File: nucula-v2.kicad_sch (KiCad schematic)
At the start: 0 parts

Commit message: Draft ESP32-C3 USB-C and Li-ion power schematic
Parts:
- added C1, C2, C4, C5, C6, C9: 22uF, Capacitor_SMD:C_0805_2012Metric, symbol Device:C
- added C10, C11, C13, C14: 100nF, Capacitor_SMD:C_0603_1608Metric, symbol Device:C
- added C12: 1uF, Capacitor_SMD:C_0603_1608Metric, symbol Device:C
- added C3: 22pF, Capacitor_SMD:C_0603_1608Metric, symbol Device:C
- added C7, C8: DNP / USB tune, Capacitor_SMD:C_0603_1608Metric, symbol Device:C
- added D1, D2: SS14, Diode_SMD:D_SMA, symbol Device:D_Schottky
- added D3: CHARGE (red), LED_SMD:LED_0603_1608Metric, symbol Device:LED
- added J1: USB4105-GF-A, Connector_USB:USB_C_Receptacle_GCT_USB4105-xx-A_16P_TopMnt_Horizontal, symbol Connector:USB_C_Receptacle_USB2.0_16P
- added J2: JST-PH / 1S Li-ion, Connector_JST:JST_PH_B2B-PH-K_1x02_P2.00mm_Vertical, symbol Connector_Generic:Conn_01x02
- added L1: 2.2uH, Nucula_Project:L_Taiyo-Yuden_NR-30xx, symbol Device:L
- added Q1: IRLML6402, Package_TO_SOT_SMD:SOT-23, symbol Transistor_FET:IRLML6402
- added Q2: BSS138, Package_TO_SOT_SMD:SOT-23, symbol Transistor_FET:BSS138
- added R1, R2: 5.1k, Resistor_SMD:R_0603_1608Metric, symbol Device:R
- added R10, R11, R3, R5, R8, R9: 10k, Resistor_SMD:R_0603_1608Metric, symbol Device:R
- added R12, R13: 22R, Resistor_SMD:R_0603_1608Metric, symbol Device:R
- added R14: 100R, Resistor_SMD:R_0603_1608Metric, symbol Device:R
- added R15, R16: 470k, Resistor_SMD:R_0603_1608Metric, symbol Device:R
- added R17, R18: 100k, Resistor_SMD:R_0603_1608Metric, symbol Device:R
- added R4: 2.2k, Resistor_SMD:R_0603_1608Metric, symbol Device:R
- added R6: 220k, Resistor_SMD:R_0603_1608Metric, symbol Device:R
- added R7: 48.7k, Resistor_SMD:R_0603_1608Metric, symbol Device:R
- added SW1: RESET, Button_Switch_SMD:SW_SPST_B3U-1000P, symbol Switch:SW_Push
- added SW2: BOOT, Button_Switch_SMD:SW_SPST_B3U-1000P, symbol Switch:SW_Push
- added U1: TP4054-42-SOT235, Package_TO_SOT_SMD:SOT-23-5, symbol Nucula_Project:TP4054-42-SOT235
- added U2: SY8089AAAC, Package_TO_SOT_SMD:SOT-23-5, symbol Nucula_Project:SY8089AAAC
- added U3: ESP32-C3-WROOM-02-N4, Nucula_Project:ESP32-C3-WROOM-02-N4, symbol Nucula_Project:ESP32-C3-WROOM-02-N4
- added U4: USBLC6-2SC6, Package_TO_SOT_SMD:SOT-23-6, symbol Power_Protection:USBLC6-2SC6
- added U5: TLV803EA30DCKR, Package_TO_SOT_SMD:SOT-323_SC-70, symbol Nucula_Project:TLV803EA30DCKR
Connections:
- new net: C8.1, R13.2, U3.14 (IO19)
- new net: L1.1, U2.3 (LX)
- new net: C7.1, R12.2, U3.13 (IO18)
- new net: J1.A5 (CC1), R1.1
- new net: J1.B5 (CC2), R2.1
- new net: R4.1, U1.1 (~{CHRG})
- new net: R3.1, U1.5 (PROG)
- new net: D3.1 (K), R4.2
- new net: R14.2, SW2.1
- new net +3V3: C10.1, C11.1, C3.1, C5.1, C6.1, C9.1, L1.2, R10.1, R11.1, R17.1, R6.1, R8.1, R9.1, U3.1 (3V3), U5.3 (VDD)
- new net BOOT_N: R11.2, R14.1, U3.8 (IO9)
- new net BUCK_FB: C3.2, R6.2, R7.1, U2.5 (FB)
- new net ESP_EN: C12.1, R8.2, SW1.1, U3.2 (EN), U5.2 (~{RESET})
- new net GND: C1.2, C10.2, C11.2, C12.2, C13.2, C14.2, C2.2, C4.2, C5.2, C6.2, C7.2, C8.2, C9.2, J1.A1 (GND), J1.A12 (GND), J1.B1 (GND), J1.B12 (GND), J1.SH (SHIELD), J2.2 (Pin_2), Q2.2 (S), R1.2, R16.2, R18.2, R2.2, R3.2, R5.2, R7.2, SW1.2, SW2.2, U1.2 (GND), U2.2 (GND), U3.19 (GND), U3.9 (GND), U4.2 (GND), U5.1 (GND)
- new net STRAP_GPIO2: R9.2, U3.16 (IO2)
- new net STRAP_GPIO8: R10.2, U3.7 (IO8)
- new net USB_5V: C1.1, D1.1 (K), D2.2 (A), D3.2 (A), Q1.1 (G), R5.1, U1.4 (VCC)
- new net USB_D+: J1.A6 (D+), J1.B6 (D+), U4.3 (I/O2)
- new net USB_D-: J1.A7 (D-), J1.B7 (D-), U4.1 (I/O1)
- new net USB_ESD_D+: R13.1, U4.4 (I/O2)
- new net USB_ESD_D-: R12.1, U4.6 (I/O1)
- new net USB_PRESENT_N: Q2.3 (D), R17.2, U3.17 (IO1)
- new net VBAT: C2.1, J2.1 (Pin_1), Q1.3 (D), R15.1, U1.3 (BAT)
- new net VBAT_ADC: C13.1, R15.2, R16.1, U3.18 (IO0)
- new net VBUS: C14.1, D1.2 (A), J1.A4 (VBUS), J1.A9 (VBUS), J1.B4 (VBUS), J1.B9 (VBUS), Q2.1 (G), R18.1, U4.5 (VBUS)
- new net VSYS: C4.1, D2.1 (K), Q1.2 (S), U2.1 (EN), U2.4 (IN)
- no-connect marks 0 -> 10
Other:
- note added: "01 USB 2.0 device / 5 V sink"
- note added: "02 4.2 V / 100 mA charger"
- note added: "03 USB-priority supply / 3.31 V buck"
- note added: "04 ESP32-C3-WROOM-02-N4 / native USB"
- note added: "05 Reset, undervoltage and boot straps"
- note added: "06 Battery and USB presence sensing"
- note added: "3.08 V supervisor, open-drain reset, ~200 ms delay. EN: 10k / 1uF. 3.08 V nominal low-voltage reset."
- note added: "CC1 / CC2: independent 5.1k Rd. No USB-PD. Route D+/D- as a 90 ohm differential pair. Place U4 at connector; R12/R13 at module. See design notes for USB current / inrush limits."
- note added: "DRAFT / before PCB: Confirm protected battery and JST polarity. Validate USB current, inrush, suspend and ESD. Verify regulator layout, capacitor bias and load steps. Reference: Olimex ESP32-C3-DevKit-Lipo Rev C. See docs/power-design.md for sources and limits."
- note added: "ERC source declarations"
- note added: "Hold BOOT; tap RESET to enter ROM download mode. GPIO8 must stay high while GPIO9 is low. No large capacitor on GPIO9."
- note added: "NUCULA v2 / USB-C, Li-ion power and ESP32-C3"
- note added: "Protected 1S Li-ion/LiPo only (4.2 V full). J2 pin 1 = BAT+; pin 2 = GND. Check pack polarity! 100 mA nominal; termination ~10 mA. No cell-temperature input. Confirm battery rating."
- note added: "Q1 drain = battery, source = VSYS. Body diode points VBAT -> VSYS. USB load bypasses charge-current sensing."
- note added: "USB D- = GPIO18 (pin 13); D+ = GPIO19 (pin 14). No UART bridge. Unused GPIOs deliberately marked NC. Keep antenna clear; bond EP pin 19 and pin 9 to ground. Use ADC1 GPIO0 for battery sensing (not ADC2)."
- note added: "VBAT_ADC = VBAT / 2, max ~2.15 V incl. tolerances. ADC1 GPIO0: use calibrated 11/12 dB attenuation. Divider load ~4.5 uA; allow >=120 ms to settle. USB_PRESENT_N: GPIO1 LOW when VBUS is present. Firmware must disable USB attach when VBUS is absent. Q2 isolates 5 V VBUS from the 3.3 V GPIO supply."
- note added: "VOUT = 3.31 V; R6 / R7: 0.1% precision 500 mA rail design target; validate transients. Buck only: low battery causes dropout / reset. C5 + C6: 44 uF nominal; verify DC-bias derating."
- title: (none) -> Nucula v2 - USB-C, battery power and ESP32-C3

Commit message: Set 400 mAh battery target with JST-PH connector
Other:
- note added: "Protected 1S LiPo, ~400mAh (3.7V nom / 4.2V full). J2: JST-PH 2.0mm; pin 1 = BAT+; pin 2 = GND. 100mA charge = 0.25C at 400mAh; ~10mA termination. Confirm pack polarity and ratings; no cell-temp input."
- note removed: "Protected 1S Li-ion/LiPo only (4.2 V full). J2 pin 1 = BAT+; pin 2 = GND. Check pack polarity! 100 mA nominal; termination ~10 mA. No cell-temperature input. Confirm battery rating."
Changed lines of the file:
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@@
   (title_block
     (title "Nucula v2 - USB-C, battery power and ESP32-C3")
-    (date "2026-09-19")
+    (date "2026-09-20")
     (rev "A-draft")
     (comment 1 "Adapted from Olimex ESP32-C3-DevKit-Lipo Rev C; CERN-OHL-S-2.0")
@@
     )
   )
-  (text "Protected 1S Li-ion/LiPo only (4.2 V full).\nJ2 pin 1 = BAT+; pin 2 = GND. Check pack polarity!\n100 mA nominal; termination ~10 mA.\nNo cell-temperature input. Confirm battery rating."
+  (text "Protected 1S LiPo, ~400mAh (3.7V nom / 4.2V full).\nJ2: JST-PH 2.0mm; pin 1 = BAT+; pin 2 = GND.\n100mA charge = 0.25C at 400mAh; ~10mA termination.\nConfirm pack polarity and ratings; no cell-temp input."
     (at 144.78 91.44 0)
     (effects

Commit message: Integrate NFC, OLED and breakaway I2C keyboard
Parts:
- removed C1, C2, C4, C5, C6, C9: 22uF, Capacitor_SMD:C_0805_2012Metric, symbol Device:C
- removed C10, C11, C13, C14: 100nF, Capacitor_SMD:C_0603_1608Metric, symbol Device:C
- removed C12: 1uF, Capacitor_SMD:C_0603_1608Metric, symbol Device:C
- removed C3: 22pF, Capacitor_SMD:C_0603_1608Metric, symbol Device:C
- removed C7, C8: DNP / USB tune, Capacitor_SMD:C_0603_1608Metric, symbol Device:C
- removed D1, D2: SS14, Diode_SMD:D_SMA, symbol Device:D_Schottky
- removed D3: CHARGE (red), LED_SMD:LED_0603_1608Metric, symbol Device:LED
- removed J1: USB4105-GF-A, Connector_USB:USB_C_Receptacle_GCT_USB4105-xx-A_16P_TopMnt_Horizontal, symbol Connector:USB_C_Receptacle_USB2.0_16P
- removed J2: JST-PH / 1S Li-ion, Connector_JST:JST_PH_B2B-PH-K_1x02_P2.00mm_Vertical, symbol Connector_Generic:Conn_01x02
- removed L1: 2.2uH, Nucula_Project:L_Taiyo-Yuden_NR-30xx, symbol Device:L
- removed Q1: IRLML6402, Package_TO_SOT_SMD:SOT-23, symbol Transistor_FET:IRLML6402
- removed Q2: BSS138, Package_TO_SOT_SMD:SOT-23, symbol Transistor_FET:BSS138
- removed R1, R2: 5.1k, Resistor_SMD:R_0603_1608Metric, symbol Device:R
- removed R10, R11, R3, R5, R8, R9: 10k, Resistor_SMD:R_0603_1608Metric, symbol Device:R
- removed R12, R13: 22R, Resistor_SMD:R_0603_1608Metric, symbol Device:R
- removed R14: 100R, Resistor_SMD:R_0603_1608Metric, symbol Device:R
- removed R15, R16: 470k, Resistor_SMD:R_0603_1608Metric, symbol Device:R
- removed R17, R18: 100k, Resistor_SMD:R_0603_1608Metric, symbol Device:R
- removed R4: 2.2k, Resistor_SMD:R_0603_1608Metric, symbol Device:R
- removed R6: 220k, Resistor_SMD:R_0603_1608Metric, symbol Device:R
- removed R7: 48.7k, Resistor_SMD:R_0603_1608Metric, symbol Device:R
- removed SW1: RESET, Button_Switch_SMD:SW_SPST_B3U-1000P, symbol Switch:SW_Push
- removed SW2: BOOT, Button_Switch_SMD:SW_SPST_B3U-1000P, symbol Switch:SW_Push
- removed U1: TP4054-42-SOT235, Package_TO_SOT_SMD:SOT-23-5, symbol Nucula_Project:TP4054-42-SOT235
- removed U2: SY8089AAAC, Package_TO_SOT_SMD:SOT-23-5, symbol Nucula_Project:SY8089AAAC
- removed U3: ESP32-C3-WROOM-02-N4, Nucula_Project:ESP32-C3-WROOM-02-N4, symbol Nucula_Project:ESP32-C3-WROOM-02-N4
- removed U4: USBLC6-2SC6, Package_TO_SOT_SMD:SOT-23-6, symbol Power_Protection:USBLC6-2SC6
- removed U5: TLV803EA30DCKR, Package_TO_SOT_SMD:SOT-323_SC-70, symbol Nucula_Project:TLV803EA30DCKR
- added C49: 1uF, Capacitor_SMD:C_0805_2012Metric, symbol Device:C
- added C50: 2.2uF, Capacitor_SMD:C_0805_2012Metric, symbol Device:C
- added J4: MAIN LINK / OPTIONAL, Connector_PinHeader_2.54mm:PinHeader_1x05_P2.54mm_Vertical, symbol Connector_Generic:Conn_01x05
- added R19, R20: 2.2k, Resistor_SMD:R_0603_1608Metric, symbol Device:R
- added R40: 100k, Resistor_SMD:R_0603_1608Metric, symbol Device:R
- added U9: MCP1700T-3002E/TT, Package_TO_SOT_SMD:SOT-23, symbol Regulator_Linear:MCP1700x-300xxTT
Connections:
- net +3V3: now also C49.1, J4.1 (Pin_1), R40.1, U9.3 (VI)
- net GND: now also C49.2, C50.2, J4.2 (Pin_2), U9.1 (GND)
- new net +3V0: C50.1, R19.1, R20.1, U9.2 (VO)
- new net I2C_SCL: J4.4 (Pin_4), R20.2
- new net I2C_SDA: J4.3 (Pin_3), R19.2
- new net KEY_INT_N: J4.5 (Pin_5), R40.2
- no-connect marks 10 -> 0
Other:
- added sheet Keyboard / breakaway / 0x20 (keyboard.kicad_sch)
- added sheet NFC / PN7160 / 0x28 (nfc.kicad_sch)
- added sheet OLED / SSD1309 / 0x3C (oled.kicad_sch)
- added sheet Power + ESP32-C3 (power-mcu.kicad_sch)
- note added: "3.0 V display logic and common I2C pull-ups. SSD1309 logic max = 3.3 V; existing buck worst case ~3.39 V. 3.0 V HIGH levels also meet the 3.3 V devices' thresholds. One populated pair of I2C pull-ups. Bus speed: 100 kHz. No I2C multiplexer is needed; addresses are distinct."
- note added: "Break line carries five nets only. Reconnect J4 <-> J5 after separation. J3 9-pin keyboard header remains DNP. Mechanical break line is deferred to PCB layout."
- note added: "NFC / OLED power comes from VSYS; digital logic from regulated rails. Concurrent Wi-Fi + NFC + OLED can exceed a small 400 mAh pack's rating. Confirm peak battery current and USB input power before PCB release. RF matching/coil and exact OLED flex remain intentionally provisional."
- note added: "NUCULA v2 / system interconnect"
- note removed: "01 USB 2.0 device / 5 V sink"
- note removed: "02 4.2 V / 100 mA charger"
- note removed: "03 USB-priority supply / 3.31 V buck"
- note removed: "04 ESP32-C3-WROOM-02-N4 / native USB"
- note removed: "05 Reset, undervoltage and boot straps"
- note removed: "06 Battery and USB presence sensing"
- note removed: "3.08 V supervisor, open-drain reset, ~200 ms delay. EN: 10k / 1uF. 3.08 V nominal low-voltage reset."
- note removed: "CC1 / CC2: independent 5.1k Rd. No USB-PD. Route D+/D- as a 90 ohm differential pair. Place U4 at connector; R12/R13 at module. See design notes for USB current / inrush limits."
- note removed: "DRAFT / before PCB: Confirm protected battery and JST polarity. Validate USB current, inrush, suspend and ESD. Verify regulator layout, capacitor bias and load steps. Reference: Olimex ESP32-C3-DevKit-Lipo Rev C. See docs/power-design.md for sources and limits."
- note removed: "ERC source declarations"
- note removed: "Hold BOOT; tap RESET to enter ROM download mode. GPIO8 must stay high while GPIO9 is low. No large capacitor on GPIO9."
- note removed: "NUCULA v2 / USB-C, Li-ion power and ESP32-C3"
- note removed: "Protected 1S LiPo, ~400mAh (3.7V nom / 4.2V full). J2: JST-PH 2.0mm; pin 1 = BAT+; pin 2 = GND. 100mA charge = 0.25C at 400mAh; ~10mA termination. Confirm pack polarity and ratings; no cell-temp input."
- note removed: "Q1 drain = battery, source = VSYS. Body diode points VBAT -> VSYS. USB load bypasses charge-current sensing."
- note removed: "USB D- = GPIO18 (pin 13); D+ = GPIO19 (pin 14). No UART bridge. Unused GPIOs deliberately marked NC. Keep antenna clear; bond EP pin 19 and pin 9 to ground. Use ADC1 GPIO0 for battery sensing (not ADC2)."
- note removed: "VBAT_ADC = VBAT / 2, max ~2.15 V incl. tolerances. ADC1 GPIO0: use calibrated 11/12 dB attenuation. Divider load ~4.5 uA; allow >=120 ms to settle. USB_PRESENT_N: GPIO1 LOW when VBUS is present. Firmware must disable USB attach when VBUS is absent. Q2 isolates 5 V VBUS from the 3.3 V GPIO supply."
- note removed: "VOUT = 3.31 V; R6 / R7: 0.1% precision 500 mA rail design target; validate transients. Buck only: low battery causes dropout / reset. C5 + C6: 44 uF nominal; verify DC-bias derating."
- title: Nucula v2 - USB-C, battery power and ESP32-C3 -> Nucula v2 - system interconnect

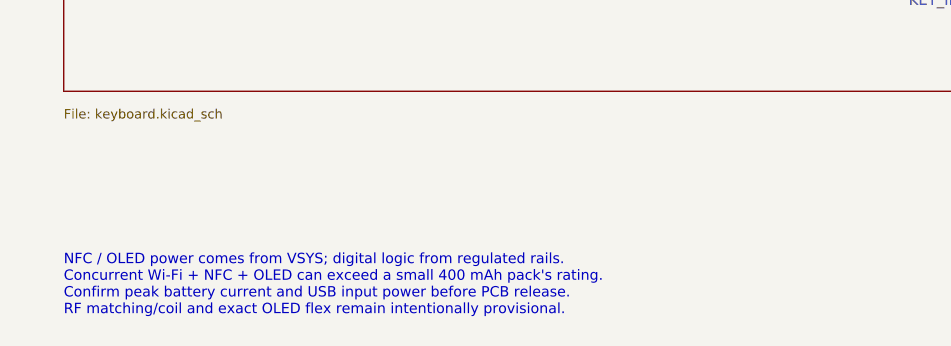
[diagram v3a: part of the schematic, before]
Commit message: Add PCB NFC coil and refine prototype component selections
Integrate a reusable 40 mm four-turn antenna footprint, calculated matching
network, hand-solder tuning pads, and a fabrication-ready bare-coil coupon.
Archive RF calculations, simulation results, reference sources, and tuning
instructions.

Select the PN7160 crystal and supply capacitors using manufacturer guidance
and DC-bias data. Record the confirmed 26-contact OLED interface and dedicated
5 V / 1.5 A USB-C source, retaining the JST-PH battery connector and deferred
battery behavior. Update the BOM, schematic PDFs, and verification tools.

Validation: native KiCad ERC reports zero violations; all current schematic
hashes match the verification report. Coil geometry, coupon DRC, RF model,
and component calculation results are archived with the design.
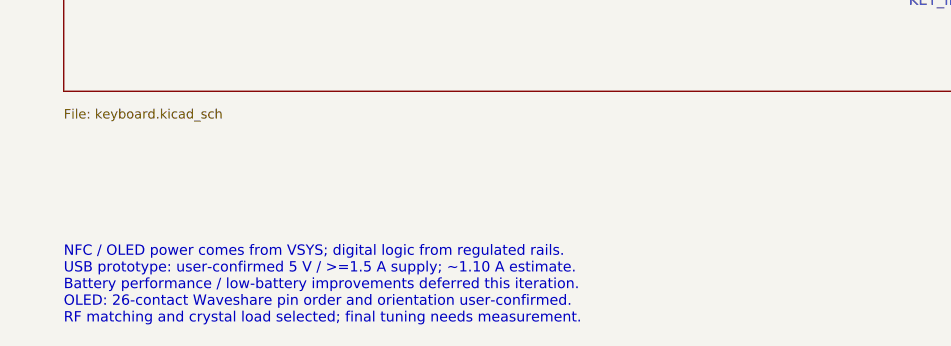
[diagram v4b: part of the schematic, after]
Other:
- note added: "NFC / OLED power comes from VSYS; digital logic from regulated rails. USB prototype: user-confirmed 5 V / >=1.5 A supply; ~1.10 A estimate. Battery performance / low-battery improvements deferred this iteration. OLED: 26-contact Waveshare pin order and orientation user-confirmed. RF matching and crystal load selected; final tuning needs measurement."
- note removed: "NFC / OLED power comes from VSYS; digital logic from regulated rails. Concurrent Wi-Fi + NFC + OLED can exceed a small 400 mAh pack's rating. Confirm peak battery current and USB input power before PCB release. RF matching/coil and exact OLED flex remain intentionally provisional."
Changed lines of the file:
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@@
     )
   )
-  (text "NFC / OLED power comes from VSYS; digital logic from regulated rails.\nConcurrent Wi-Fi + NFC + OLED can exceed a small 400 mAh pack's rating.\nConfirm peak battery current and USB input power before PCB release.\nRF matching/coil and exact OLED flex remain intentionally provisional."
+  (text "NFC / OLED power comes from VSYS; digital logic from regulated rails.\nUSB prototype: user-confirmed 5 V / >=1.5 A supply; ~1.10 A estimate.\nBattery performance / low-battery improvements deferred this iteration.\nOLED: 26-contact Waveshare pin order and orientation user-confirmed.\nRF matching and crystal load selected; final tuning needs measurement."
     (at 20.32 270.51 0)
     (effects

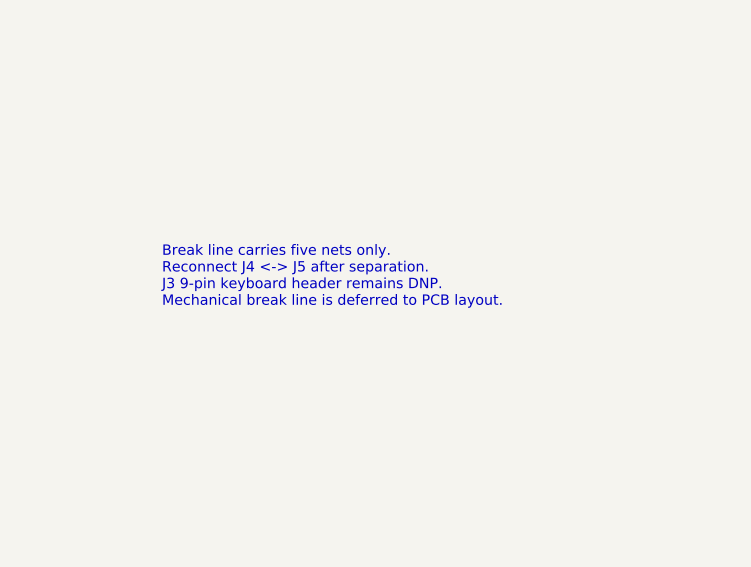
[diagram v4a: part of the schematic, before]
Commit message: Keep keypad signals on center seven header pins
Retain the DNP nine-pin header with pins 1 and 9 isolated. Map pins 2-8
to PCF8574 P0-P6, preserving the early prototype's seven-contact order,
and leave P7 unconnected.

Document the researched keypad matrix mapping and scanning behavior.
Update schematic notes, connectivity checks, BOM, verification report,
and schematic PDF.

Validation: zero native KiCad ERC violations; seven-contact mapping
matches the early netlist; isolated pins and DNP status verified;
updated schematic pages visually inspected.
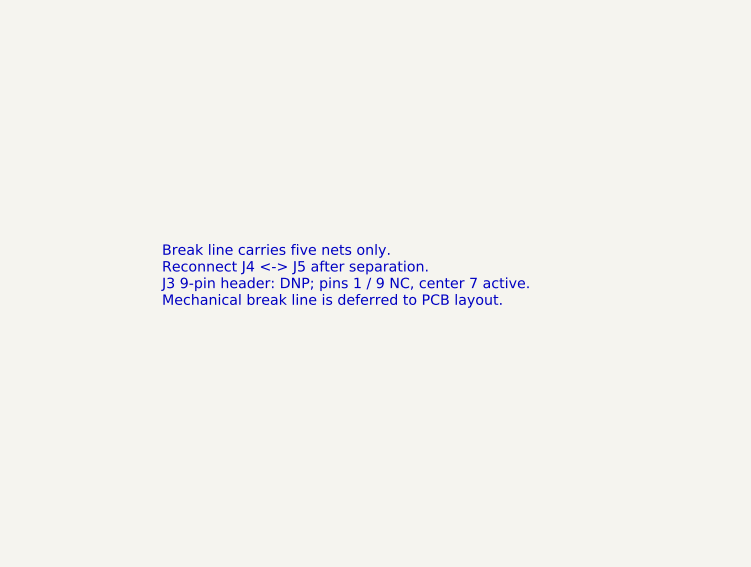
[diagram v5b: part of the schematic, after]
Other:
- note added: "Break line carries five nets only. Reconnect J4 <-> J5 after separation. J3 9-pin header: DNP; pins 1 / 9 NC, center 7 active. Mechanical break line is deferred to PCB layout."
- note removed: "Break line carries five nets only. Reconnect J4 <-> J5 after separation. J3 9-pin keyboard header remains DNP. Mechanical break line is deferred to PCB layout."
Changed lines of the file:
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@@
     )
   )
-  (text "Break line carries five nets only.\nReconnect J4 <-> J5 after separation.\nJ3 9-pin keyboard header remains DNP.\nMechanical break line is deferred to PCB layout."
+  (text "Break line carries five nets only.\nReconnect J4 <-> J5 after separation.\nJ3 9-pin header: DNP; pins 1 / 9 NC, center 7 active.\nMechanical break line is deferred to PCB layout."
     (at 304.8 210.82 0)
     (effects
